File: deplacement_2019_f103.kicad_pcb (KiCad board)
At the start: 2 copper layers, 52.1 x 87 mm, 30 parts, among them J1 Alim logique, J2 Connecteur Gauche, J3 Connecteur Droit, J4 Conn_01x05, J5 Conn_01x05, J6 PWM output, J7 PWM output, J8 Liaison serie, Q1 PMF370XN, Q2 PMF370XN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

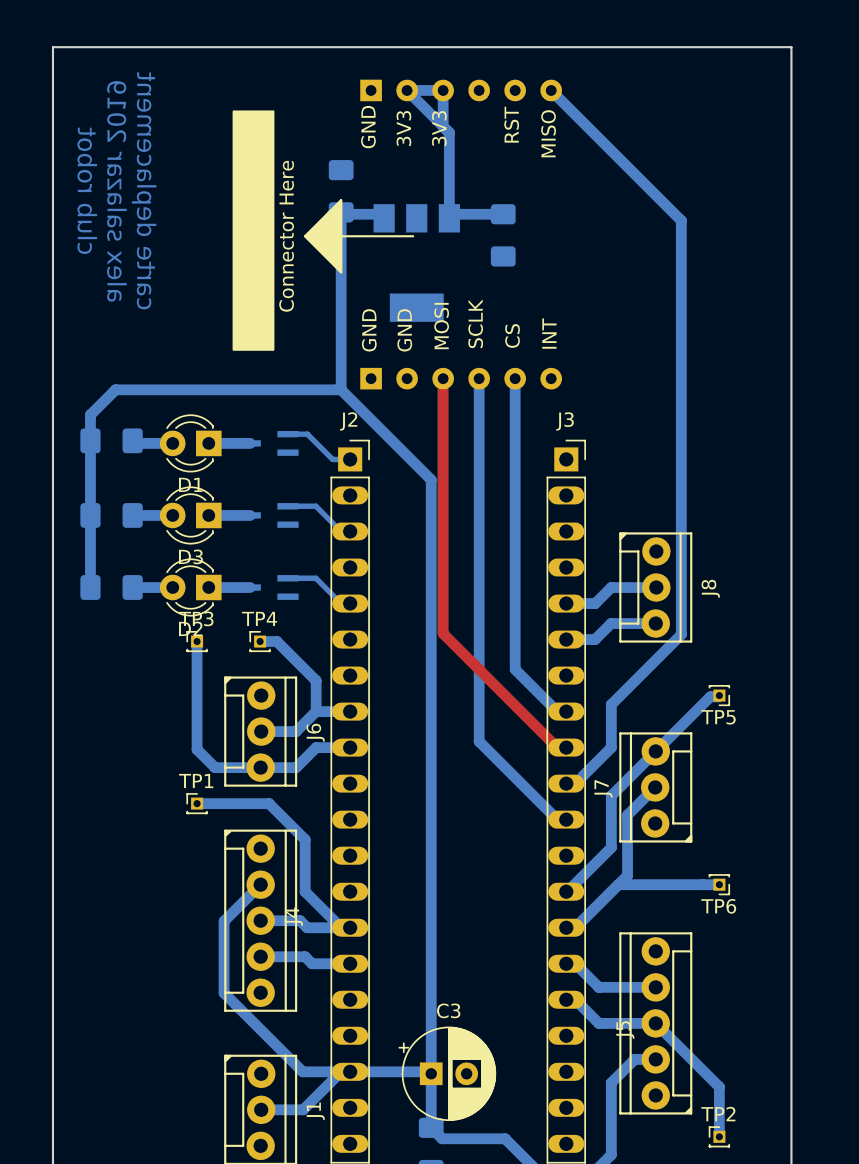
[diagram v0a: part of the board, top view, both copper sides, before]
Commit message: Fix wrong pinout for PWM pins
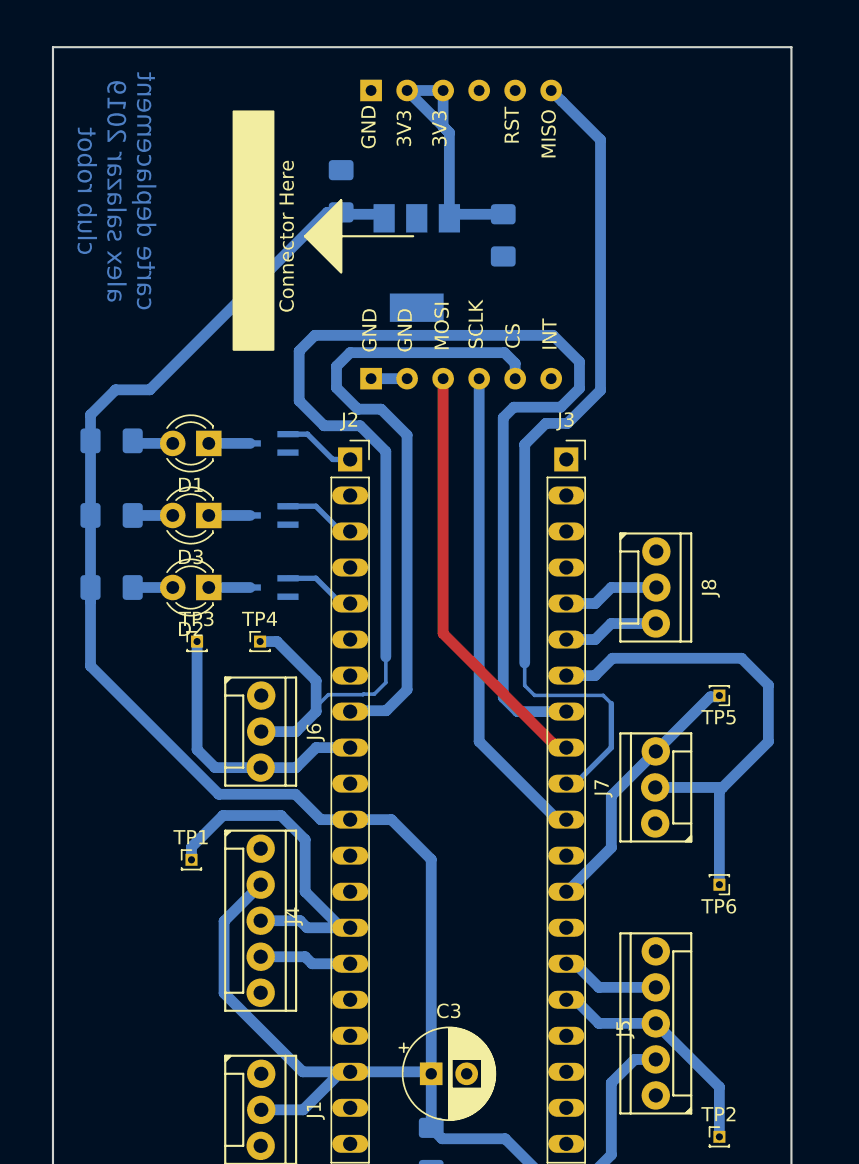
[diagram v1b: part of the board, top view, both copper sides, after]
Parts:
- moved TP1 3.98 mm to (105.7, 104.3)
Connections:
- J2 pad 11: Net-(J2-Pad11) -> +5V
- J2 pad 8: /motor_left_PWM -> /CS
- J3 pad 14: /motor_right_PWM -> GND
- J3 pad 7: Net-(J3-Pad7) -> /motor_right_PWM
- J3 pad 8: /CS -> /motor_left_PWM
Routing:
- net /motor_left_PWM: track 14.1 -> 98.8 mm
- net /CS: track 25.3 -> 44.9 mm
- net /motor_right_PWM: track 24.3 -> 35.8 mm
- net +5V: track 158.6 -> 150.7 mm
- net /MISO: track 55.1 -> 60.5 mm
- net GND: track 0.00 -> 2.54 mm
- net /qei_left_A: track 23.1 -> 25.0 mm

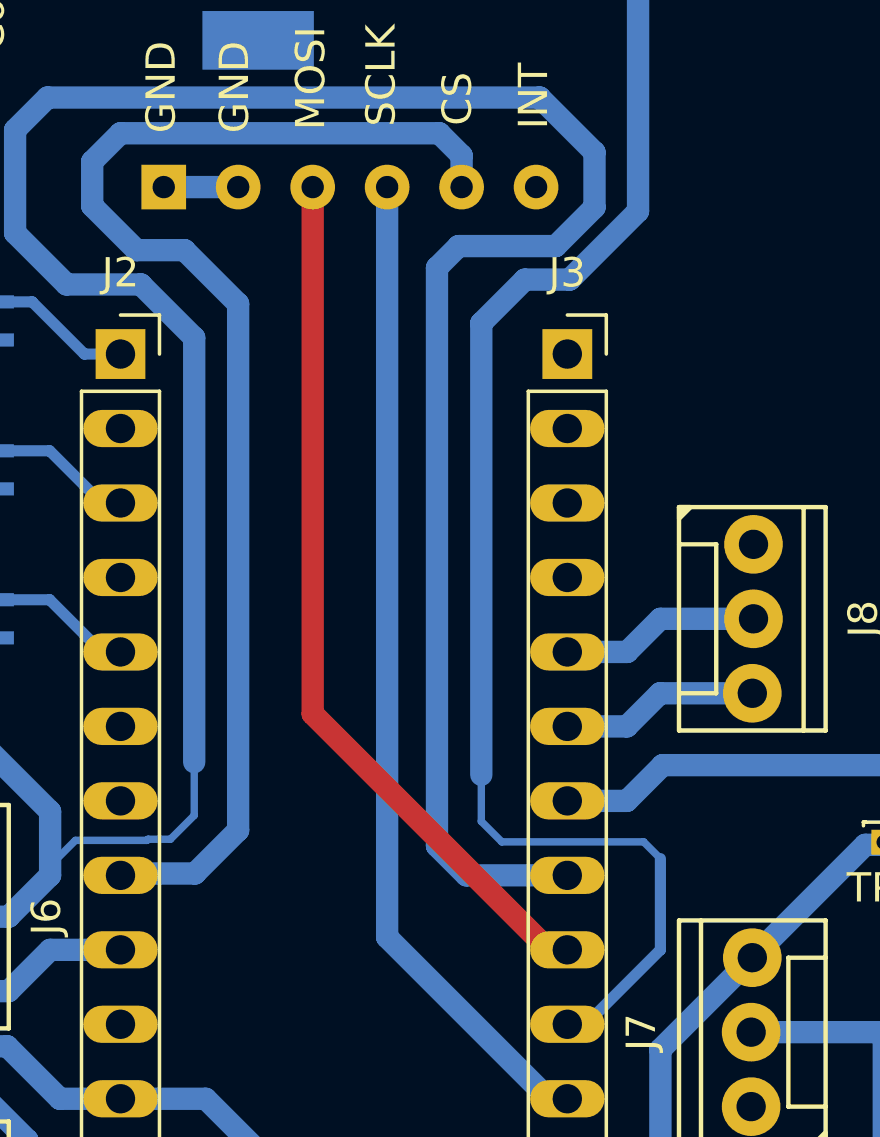
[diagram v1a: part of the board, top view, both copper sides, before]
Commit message: Add version number on schematic and PCB Add vias for top cables
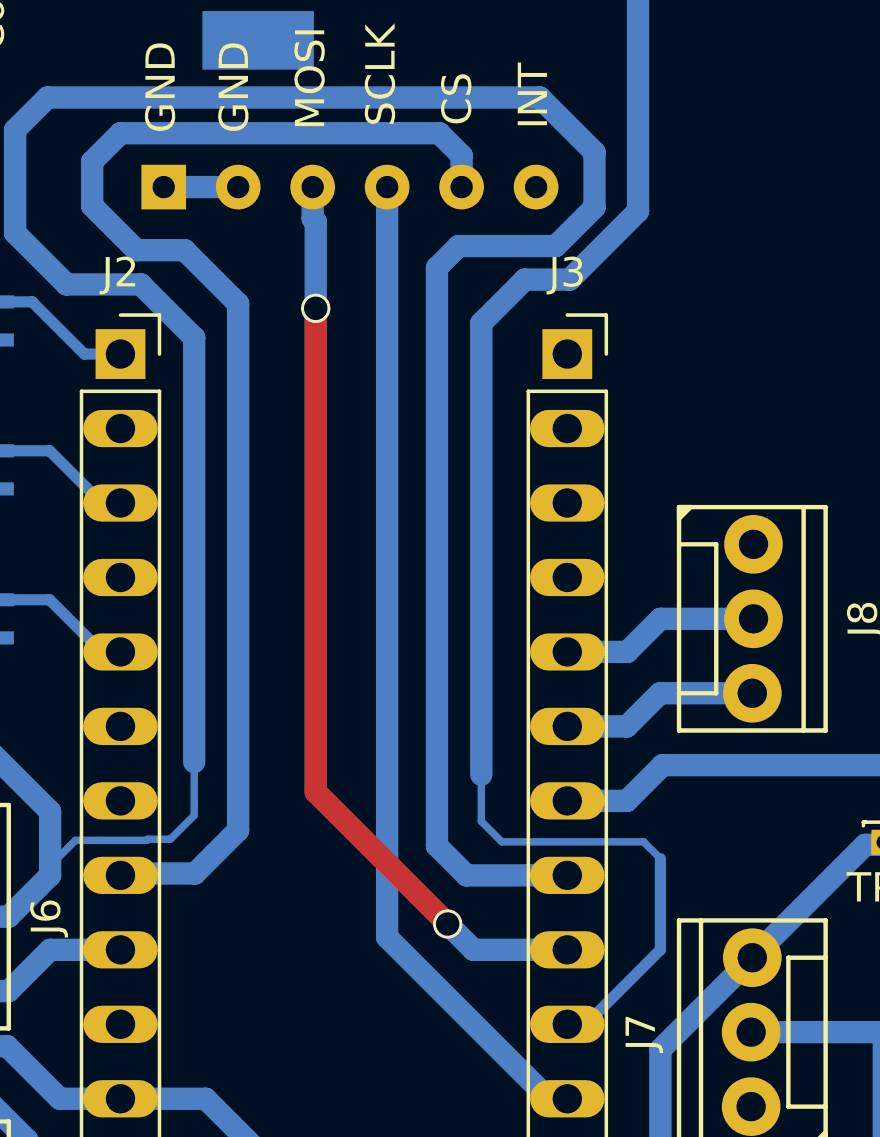
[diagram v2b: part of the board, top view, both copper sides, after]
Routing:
- net /MOSI: track 30.0 -> 32.1 mm, vias 0 -> 2
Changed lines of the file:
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@@
-(kicad_pcb (version 20171130) (host pcbnew 5.0.1)
+(kicad_pcb (version 20171130) (host pcbnew 5.1.1)
   (general
     (thickness 1.6)
     (drawings 14)
-    (tracks 170)
+    (tracks 179)
     (zones 0)
     (modules 30)
@@
   )
   (page A4)
+  (title_block
+    (title "Carte Déplacement")
+    (date 2019-05-16)
+    (rev v1)
+    (company "Club Robot")
+  )
   (layers
     (0 F.Cu signal)
@@
     (zone_45_only no)
     (trace_min 0.2)
-    (segment_width 0.2)
-    (edge_width 0.15)
     (via_size 0.8)
     (via_drill 0.4)
@@
     (uvia_min_size 0.2)
     (uvia_min_drill 0.1)
+    (edge_width 0.15)
+    (segment_width 0.2)
     (pcb_text_width 0.3)
     (pcb_text_size 1.5 1.5)
@@
   (segment (start 125.935 70.365) (end 125.935 95.95) (width 0.762) (layer B.Cu) (net 30) (status 10))
   (segment (start 131.445 96.38) (end 132.08 96.38) (width 0.762) (layer F.Cu) (net 31) (status 30))
-  (segment (start 123.395 88.33) (end 131.445 96.38) (width 0.762) (layer F.Cu) (net 31) (status 20))
-  (segment (start 123.395 70.365) (end 123.395 88.33) (width 0.762) (layer F.Cu) (net 31) (status 10))
+  (segment (start 123.395 71.44263) (end 123.5 71.54763) (width 0.762) (layer B.Cu) (net 31))
+  (segment (start 123.395 70.365) (end 123.395 71.44263) (width 0.762) (layer B.Cu) (net 31))
+  (segment (start 123.5 71.54763) (end 123.5 74.5) (width 0.762) (layer B.Cu) (net 31))
+  (segment (start 123.5 74.5) (end 123.5 74.5) (width 0.762) (layer B.Cu) (net 31))
+  (via (at 123.5 74.5) (size 1) (drill 0.8) (layers F.Cu B.Cu) (net 31))
+  (segment (start 132.08 96.38) (end 128.88 96.38) (width 0.762) (layer B.Cu) (net 31))
+  (segment (start 128.88 96.38) (end 128 95.5) (width 0.762) (layer B.Cu) (net 31))
+  (segment (start 128 95.5) (end 128 95.5) (width 0.762) (layer B.Cu) (net 31))
+  (via (at 128 95.5) (size 1) (drill 0.8) (layers F.Cu B.Cu) (net 31))
+  (segment (start 123.5 91) (end 128 95.5) (width 0.762) (layer F.Cu) (net 31))
+  (segment (start 123.5 74.5) (end 123.5 91) (width 0.762) (layer F.Cu) (net 31))
   (segment (start 132.715 111.62) (end 132.08 111.62) (width 0.762) (layer B.Cu) (net 42) (status 30))
   (segment (start 134.3815 113.2865) (end 132.715 111.62) (width 0.762) (layer B.Cu) (net 42) (status 20))

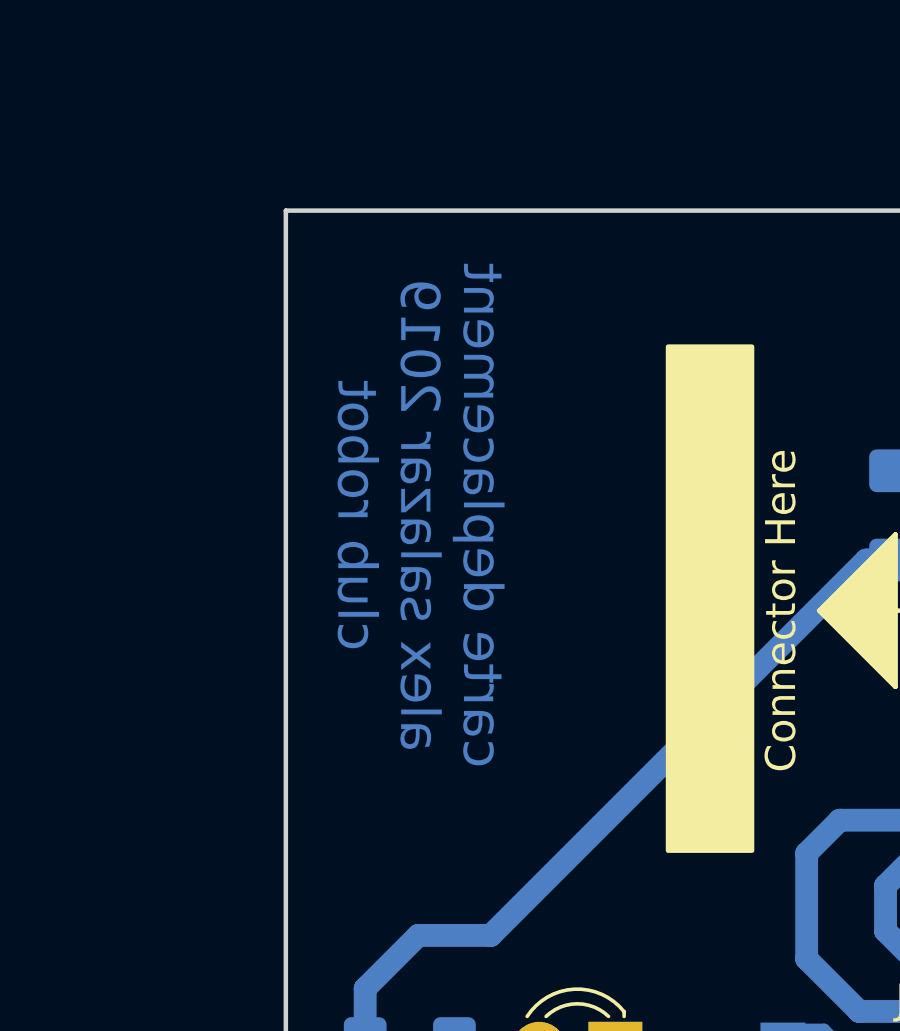
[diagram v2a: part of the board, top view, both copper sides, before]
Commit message: Add missing version number on pcb
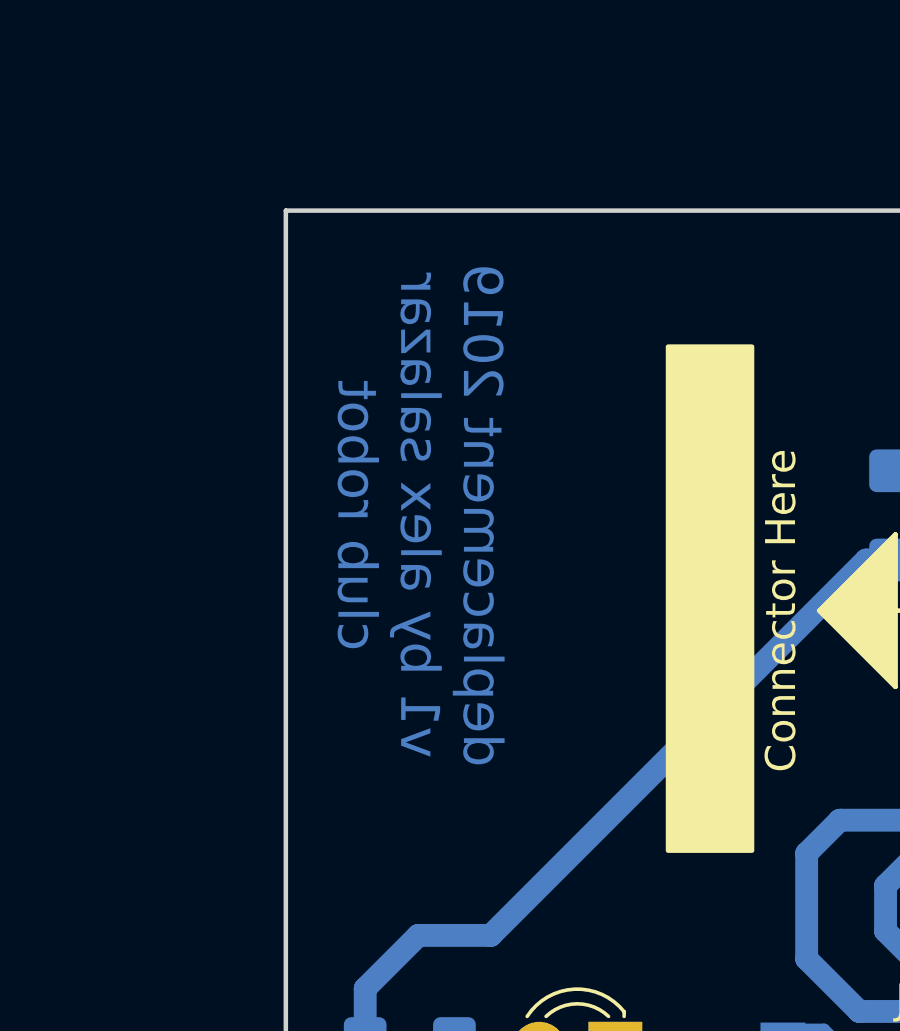
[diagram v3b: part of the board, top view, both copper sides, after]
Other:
- board text added: "deplacement 2019 v1 by alex salazar club robot"
- board text removed: "carte deplacement alex salazar 2019 club robot"
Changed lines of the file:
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@@
   (gr_line (start 95.885 46.99) (end 147.955 46.99) (layer Edge.Cuts) (width 0.15))
   (gr_line (start 95.885 46.99) (end 95.885 133.985) (layer Edge.Cuts) (width 0.15))
-  (gr_text "carte deplacement\nalex salazar 2019\nclub robot " (at 100.33 57.15 270) (layer B.Cu)
+  (gr_text "deplacement 2019 \nv1 by alex salazar\nclub robot " (at 100.33 57.15 270) (layer B.Cu)
     (effects (font (size 1.3 1.3) (thickness 0.3)) (justify mirror))
   )
